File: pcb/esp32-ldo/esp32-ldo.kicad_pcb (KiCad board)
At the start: 2 copper layers, 32 x 35.8 mm, 29 parts, among them J1 BATT, J2 PROG, J3 HALL, Q1 BC817, Q2 BC807, U1 XC6220, U2 ESP32-WROOM-32D

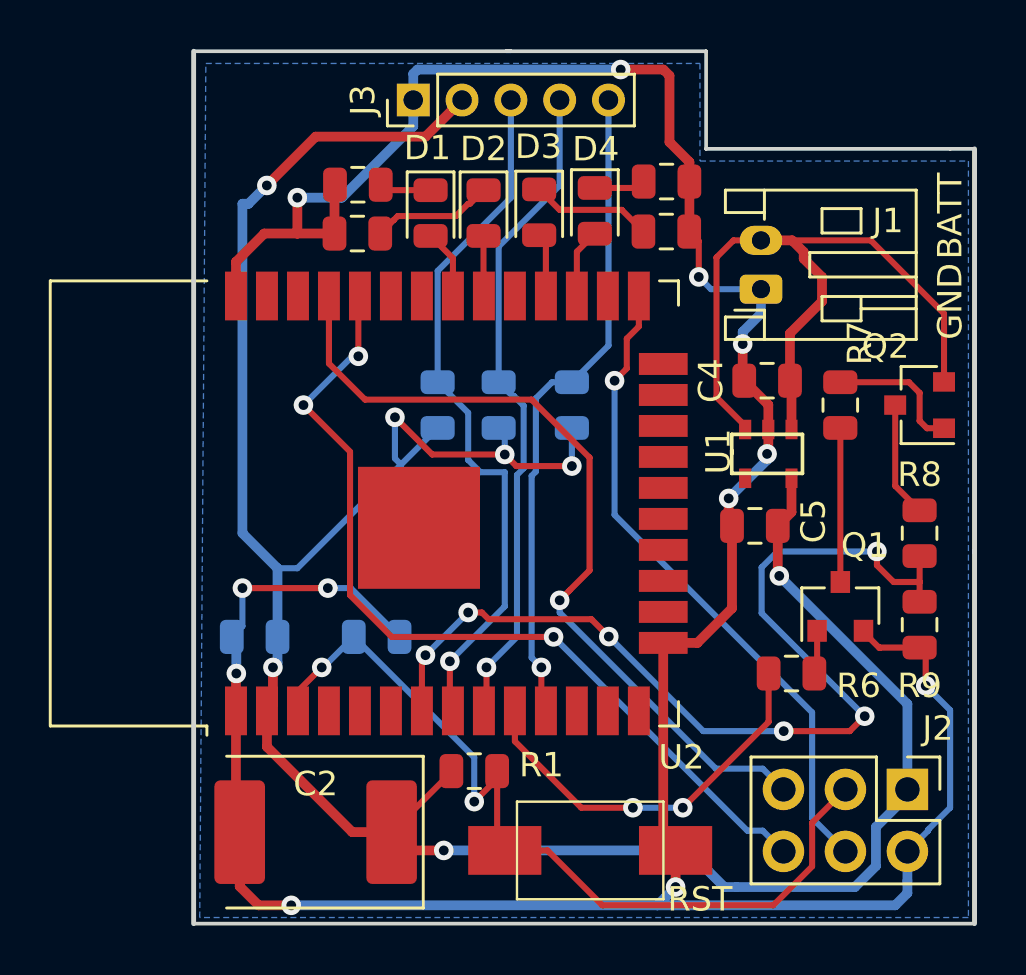
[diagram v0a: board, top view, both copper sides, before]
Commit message: update pcb size
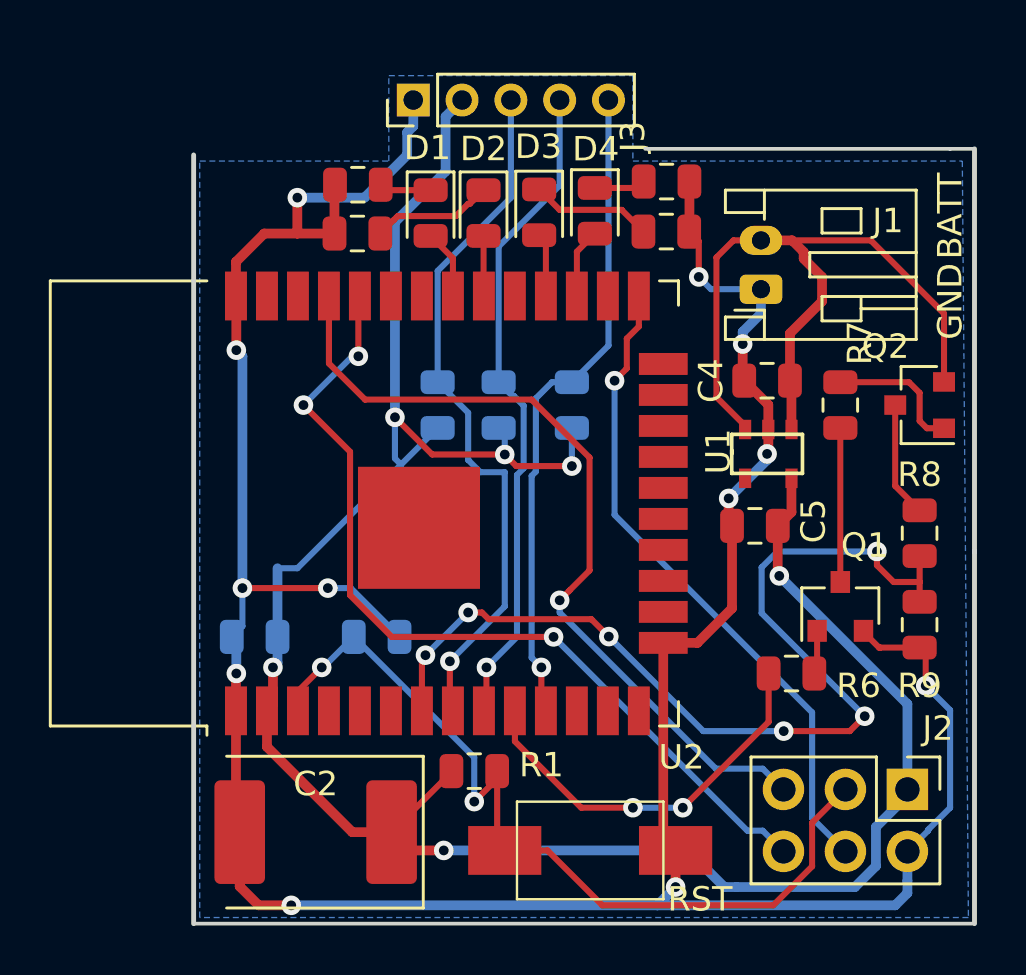
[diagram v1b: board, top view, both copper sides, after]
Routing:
- net VCC: track 106.0 -> 93.9 mm, vias 7 -> 6
- net GND: track 131.0 -> 127.2 mm
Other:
- board size 32 x 35.8 mm -> 32 x 31.8 mm
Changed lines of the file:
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@@
   (general
     (thickness 1.6)
-    (drawings 18)
-    (tracks 316)
+    (drawings 12)
+    (tracks 310)
     (zones 0)
     (modules 29)
@@
   )
   (setup
-    (last_trace_width 0.25)
+    (last_trace_width 0.4)
     (user_trace_width 0.25)
     (user_trace_width 0.4)
@@
     (descr "Through hole straight pin header, 1x05, 2.00mm pitch, single row")
     (tags "Through hole pin header THT 1x05 2.00mm single row")
-    (fp_text reference J3 (at 0 -2.06 90) (layer F.SilkS)
+    (fp_text reference J3 (at -1.5 9 270) (layer F.SilkS)
       (effects (font (size 1 1) (thickness 0.15)))
     )
@@
     )
   )
+  (gr_line (start 94.5 102.25) (end 87 102.25) (layer Eco2.User) (width 0.2))
+  (gr_line (start 94.5 98.5) (end 94.5 102.25) (layer Eco2.User) (width 0.2))
+  (gr_line (start 105.5 98.5) (end 94.5 98.5) (layer Eco2.User) (width 0.2))
+  (gr_line (start 105.5 102) (end 105.5 98.5) (layer Eco2.User) (width 0.2))
   (gr_text GND (at 118 108.25 90) (layer F.SilkS)
     (effects (font (size 1 1) (thickness 0.1)))
@@
   )
   (gr_line (start 87 133.75) (end 119 133.75) (layer Edge.Cuts) (width 0.15))
-  (gr_line (start 87 133.75) (end 87 98) (layer Edge.Cuts) (width 0.2))
+  (gr_line (start 87 133.75) (end 87 102.25) (layer Edge.Cuts) (width 0.2))
   (gr_line (start 119 118.5) (end 119 133.75) (layer Edge.Cuts) (width 0.2))
   (gr_line (start 119 102) (end 119 118.5) (layer Edge.Cuts) (width 0.2))
   (gr_line (start 118 102) (end 119 102) (layer Edge.Cuts) (width 0.15))
-  (gr_line (start 108 102) (end 118 102) (layer Edge.Cuts) (width 0.15))
-  (gr_line (start 120 94.7) (end 120 104.6) (layer Dwgs.User) (width 0.2))
-  (gr_line (start 80 87.2) (end 80 102.7) (layer Dwgs.User) (width 0.2))
-  (gr_line (start 80 100) (end 80 87.2) (layer Dwgs.User) (width 0.2))
-  (gr_line (start 108 98) (end 108 102) (layer Edge.Cuts) (width 0.15))
-  (gr_line (start 99.8 98) (end 108 98) (layer Edge.Cuts) (width 0.15))
-  (gr_line (start 100 98) (end 87 98) (layer Edge.Cuts) (width 0.15))
-  (gr_line (start 84.5 102.2) (end 103.3 102.2) (layer Dwgs.User) (width 0.2))
-  (gr_line (start 84.5 100) (end 84.5 102.2) (layer Dwgs.User) (width 0.2))
-  (gr_line (start 108 102.2) (end 101 102.2) (layer Dwgs.User) (width 0.2))
-  (gr_line (start 108 100) (end 108 102.2) (layer Dwgs.User) (width 0.2))
+  (gr_line (start 105.5 102) (end 118 102) (layer Edge.Cuts) (width 0.15))
   (segment (start 95.1125 130) (end 93.5 130) (width 0.4) (layer F.Cu) (net 1))
   (segment (start 90.005 126.505) (end 90.005 125.03) (width 0.4) (layer F.Cu) (net 1))
@@
   (segment (start 90.25 124.785) (end 90.005 125.03) (width 0.4) (layer F.Cu) (net 1))
   (segment (start 90.25 123.25) (end 90.25 124.785) (width 0.4) (layer F.Cu) (net 1))
-  (segment (start 89 104.25) (end 89 117.75) (width 0.4) (layer B.Cu) (net 1))
   (segment (start 90.4375 119.1875) (end 90.4375 122) (width 0.4) (layer B.Cu) (net 1))
-  (segment (start 89 117.75) (end 90.4375 119.1875) (width 0.4) (layer B.Cu) (net 1))
   (segment (start 111.2 117.1875) (end 110.9375 117.45) (width 0.4) (layer F.Cu) (net 1))
   (segment (start 97.5625 127.55) (end 97.5625 127.5) (width 0.25) (layer F.Cu) (net 1))
@@
   (segment (start 95.5 114.9375) (end 97 113.4375) (width 0.25) (layer B.Cu) (net 1))
   (segment (start 91.25 119.1875) (end 95.5 114.9375) (width 0.25) (layer B.Cu) (net 1))
-  (via (at 90 103.5) (size 0.8) (drill 0.4) (layers F.Cu B.Cu) (net 1))
-  (segment (start 89.25 104.25) (end 90 103.5) (width 0.4) (layer B.Cu) (net 1))
-  (segment (start 89 104.25) (end 89.25 104.25) (width 0.4) (layer B.Cu) (net 1))
-  (segment (start 90 103.5) (end 92 101.5) (width 0.4) (layer F.Cu) (net 1))
-  (segment (start 96.5 101.5) (end 98 100) (width 0.4) (layer F.Cu) (net 1))
-  (segment (start 92 101.5) (end 96.5 101.5) (width 0.4) (layer F.Cu) (net 1))
+  (segment (start 97.325001 100.674999) (end 97.325001 102.924999) (width 0.4) (layer B.Cu) (net 1))
+  (segment (start 98 100) (end 97.325001 100.674999) (width 0.4) (layer B.Cu) (net 1))
+  (segment (start 95.25 105) (end 95.25 113) (width 0.4) (layer B.Cu) (net 1))
+  (segment (start 97.325001 102.924999) (end 95.25 105) (width 0.4) (layer B.Cu) (net 1))
   (segment (start 110.25 105.75) (end 109.975 105.75) (width 0.25) (layer F.Cu) (net 3))
   (segment (start 110.25 105.75) (end 114.75 105.75) (width 0.25) (layer F.Cu) (net 3))
@@
   (segment (start 107.3175 105.38) (end 107.3075 105.39) (width 0.4) (layer F.Cu) (net 4))
   (segment (start 107.3175 103.34) (end 107.3175 105.38) (width 0.4) (layer F.Cu) (net 4))
-  (segment (start 107.3175 103.34) (end 107.3175 102.54) (width 0.4) (layer F.Cu) (net 4))
-  (segment (start 106.5 99) (end 106.25 98.75) (width 0.4) (layer F.Cu) (net 4))
-  (segment (start 107.3175 102.54) (end 106.5 101.7225) (width 0.4) (layer F.Cu) (net 4))
-  (segment (start 106.5 101.7225) (end 106.5 99) (width 0.4) (layer F.Cu) (net 4))
   (segment (start 109.0625 120.8275) (end 109.0625 117.45) (width 0.4) (layer F.Cu) (net 4))
   (segment (start 107.645 122.245) (end 109.0625 120.8275) (width 0.4) (layer F.Cu) (net 4))
@@
   (segment (start 117 122.6875) (end 116.75 122.4375) (width 0.25) (layer F.Cu) (net 4))
   (segment (start 117 124) (end 117 122.6875) (width 0.25) (layer F.Cu) (net 4))
-  (via (at 104.5 98.75) (size 0.8) (drill 0.4) (layers F.Cu B.Cu) (net 4))
-  (segment (start 106.25 98.75) (end 104.5 98.75) (width 0.4) (layer F.Cu) (net 4))
-  (segment (start 96.175 98.75) (end 96 98.925) (width 0.4) (layer B.Cu) (net 4))
-  (segment (start 96 98.925) (end 96 100) (width 0.4) (layer B.Cu) (net 4))
-  (segment (start 104.5 98.75) (end 96.175 98.75) (width 0.4) (layer B.Cu) (net 4))
-  (segment (start 93.075 104) (end 91.25 104) (width 0.4) (layer B.Cu) (net 4))
   (via (at 91.25 104) (size 0.8) (drill 0.4) (layers F.Cu B.Cu) (net 4))
-  (segment (start 96 101.075) (end 93.075 104) (width 0.4) (layer B.Cu) (net 4))
-  (segment (start 96 100) (end 96 101.075) (width 0.4) (layer B.Cu) (net 4))
   (segment (start 91.25 104) (end 91.25 105.47) (width 0.4) (layer F.Cu) (net 4))
   (segment (start 91.25 105.47) (end 92.7725 105.47) (width 0.4) (layer F.Cu) (net 4))
   (segment (start 89.895 105.47) (end 91.25 105.47) (width 0.4) (layer F.Cu) (net 4))
+  (via (at 88.75 110.25) (size 0.8) (drill 0.4) (layers F.Cu B.Cu) (net 4))
+  (segment (start 89 110.5) (end 88.75 110.25) (width 0.4) (layer B.Cu) (net 4))
+  (segment (start 89 120) (end 89 110.5) (width 0.4) (layer B.Cu) (net 4))
+  (segment (start 88.75 108.045) (end 88.735 108.03) (width 0.4) (layer F.Cu) (net 4))
+  (segment (start 88.75 110.25) (end 88.75 108.045) (width 0.4) (layer F.Cu) (net 4))
+  (segment (start 96 101.075) (end 95.75 101.325) (width 0.4) (layer B.Cu) (net 4))
+  (segment (start 96 100) (end 96 101.075) (width 0.4) (layer B.Cu) (net 4))
+  (segment (start 95.75 101.325) (end 95.75 102.25) (width 0.4) (layer B.Cu) (net 4))
+  (segment (start 94 104) (end 91.25 104) (width 0.4) (layer B.Cu) (net 4))
+  (segment (start 95.75 102.25) (end 94 104) (width 0.4) (layer B.Cu) (net 4))
   (segment (start 96.355 122.895) (end 96.5 122.75) (width 0.25) (layer F.Cu) (net 5))
   (via (at 96.5 122.75) (size 0.8) (drill 0.4) (layers F.Cu B.Cu) (net 5))
@@
     (polygon
       (pts
-        (xy 87.5 98.5) (xy 107.75 98.5) (xy 107.75 102.5) (xy 118.75 102.5) (xy 118.75 133.5)
-        (xy 87.25 133.5)
+        (xy 87.25 102.5) (xy 95 102.5) (xy 95 99) (xy 105 99) (xy 105 102.5)
+        (xy 118.5 102.5) (xy 118.75 133.5) (xy 87.25 133.5)
       )
     )

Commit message: update pcb: rst button
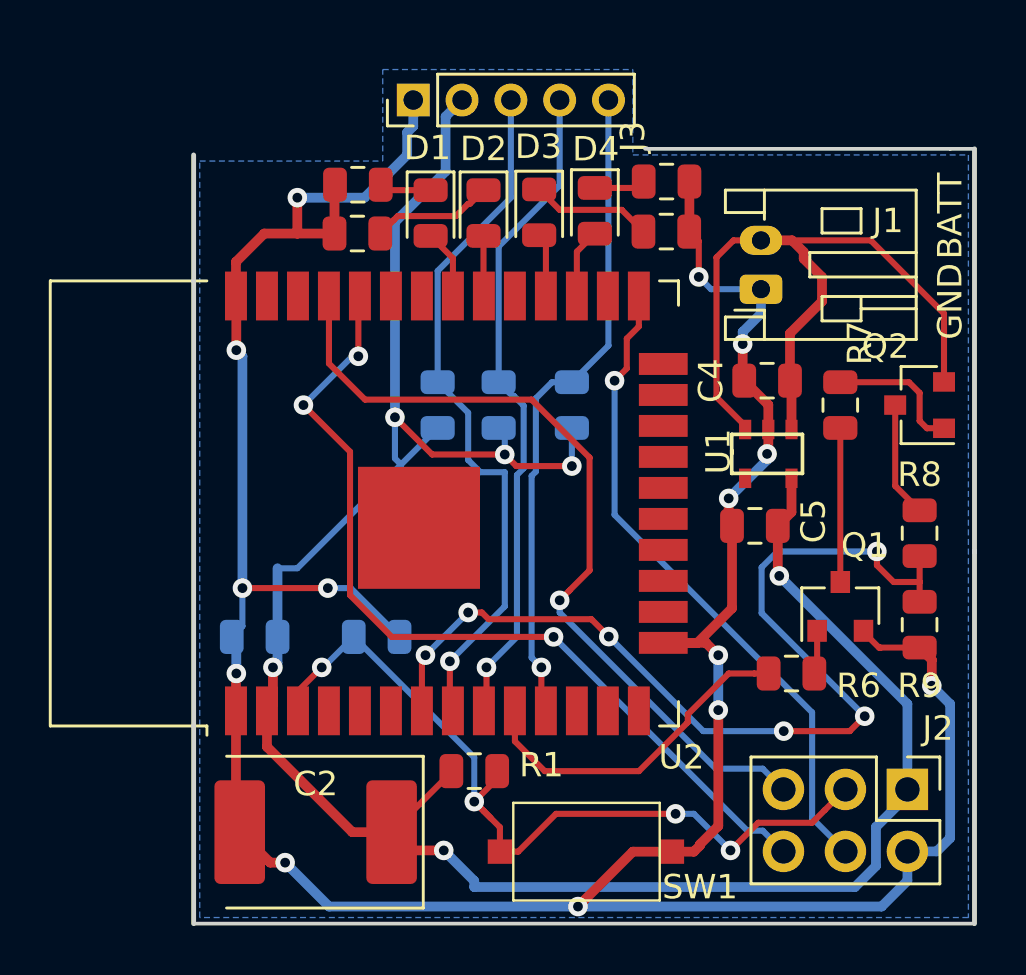
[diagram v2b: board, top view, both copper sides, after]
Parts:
- removed RST: RST, button:SMD_Button
- added SW1: RST, button:SMD_Button, F.Cu at (103.2, 131.0)
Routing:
- net GND: track 127.2 -> 132.1 mm, vias 12 -> 14
- net ENABLE_ADC: track 16.2 -> 14.0 mm, vias 2 -> 0
- net EN: track 35.7 -> 34.3 mm, vias 2 -> 4

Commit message: fix edge cuts
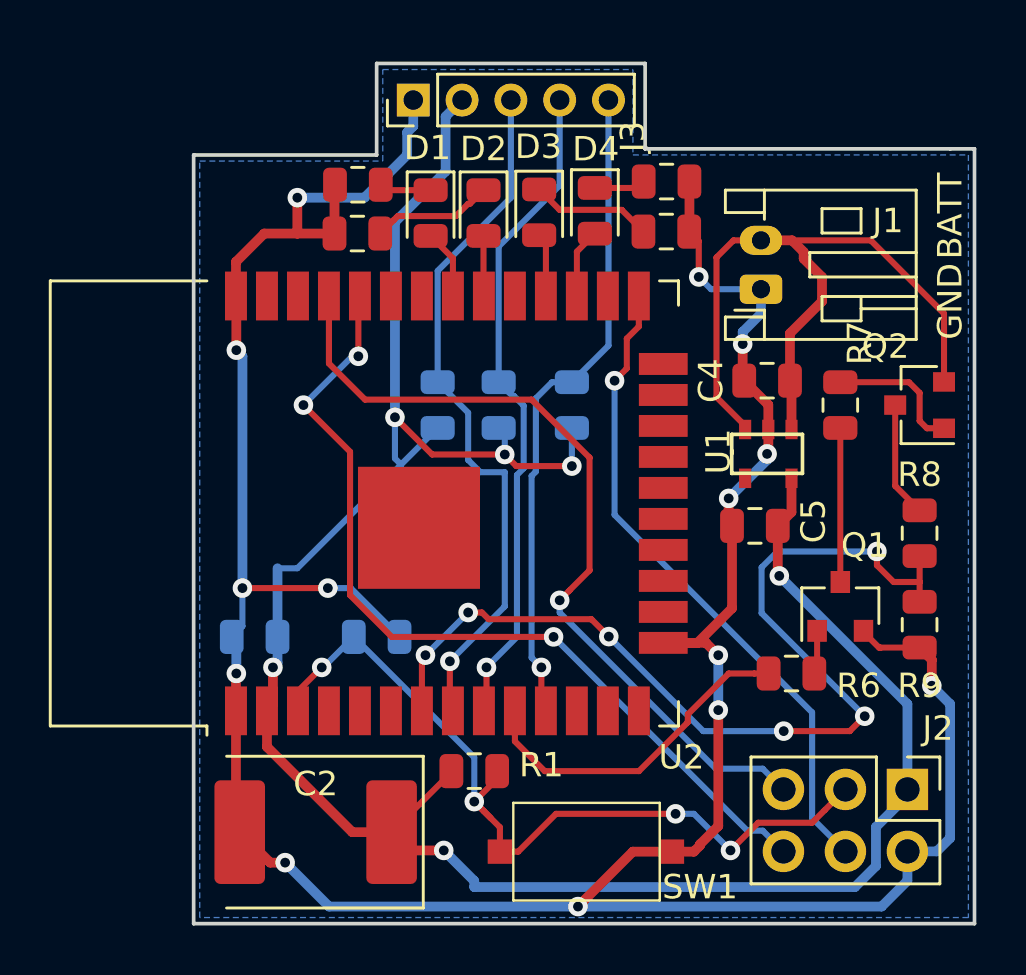
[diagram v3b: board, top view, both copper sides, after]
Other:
- board size 32 x 31.8 mm -> 32 x 35.2 mm
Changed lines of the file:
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@@
   (general
     (thickness 1.6)
-    (drawings 12)
+    (drawings 11)
     (tracks 322)
     (zones 0)
@@
   )
   (setup
-    (last_trace_width 0.4)
+    (last_trace_width 0.25)
     (user_trace_width 0.25)
     (user_trace_width 0.4)
@@
       (net 15 EN))
   )
-  (gr_line (start 94.5 102.25) (end 87 102.25) (layer Eco2.User) (width 0.2))
-  (gr_line (start 94.5 98.5) (end 94.5 102.25) (layer Eco2.User) (width 0.2))
-  (gr_line (start 105.5 98.5) (end 94.5 98.5) (layer Eco2.User) (width 0.2))
-  (gr_line (start 105.5 102) (end 105.5 98.5) (layer Eco2.User) (width 0.2))
+  (gr_line (start 94.5 98.5) (end 105.5 98.5) (layer Edge.Cuts) (width 0.15))
+  (gr_line (start 105.5 98.5) (end 105.5 102) (layer Edge.Cuts) (width 0.15))
+  (gr_line (start 94.5 102.25) (end 87 102.25) (layer Edge.Cuts) (width 0.15))
+  (gr_line (start 94.5 102.25) (end 94.5 98.5) (layer Edge.Cuts) (width 0.15))
   (gr_text GND (at 118 108.25 90) (layer F.SilkS)
     (effects (font (size 1 1) (thickness 0.1)))
@@
   )
   (gr_line (start 87 133.75) (end 119 133.75) (layer Edge.Cuts) (width 0.15))
-  (gr_line (start 87 133.75) (end 87 102.25) (layer Edge.Cuts) (width 0.2))
-  (gr_line (start 119 118.5) (end 119 133.75) (layer Edge.Cuts) (width 0.2))
-  (gr_line (start 119 102) (end 119 118.5) (layer Edge.Cuts) (width 0.2))
+  (gr_line (start 87 133.75) (end 87 102.25) (layer Edge.Cuts) (width 0.15))
+  (gr_line (start 119 102) (end 119 133.75) (layer Edge.Cuts) (width 0.15))
   (gr_line (start 118 102) (end 119 102) (layer Edge.Cuts) (width 0.15))
   (gr_line (start 105.5 102) (end 118 102) (layer Edge.Cuts) (width 0.15))
